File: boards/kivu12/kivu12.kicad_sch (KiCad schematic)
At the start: 26 parts, among them J1 P1, J10 SD, J11 GND, J12 LX2, J2 CIX, J3 BX, J4 LX1, J5 ANALOG, J6 POWER2, J7 BX, J9 POWER1

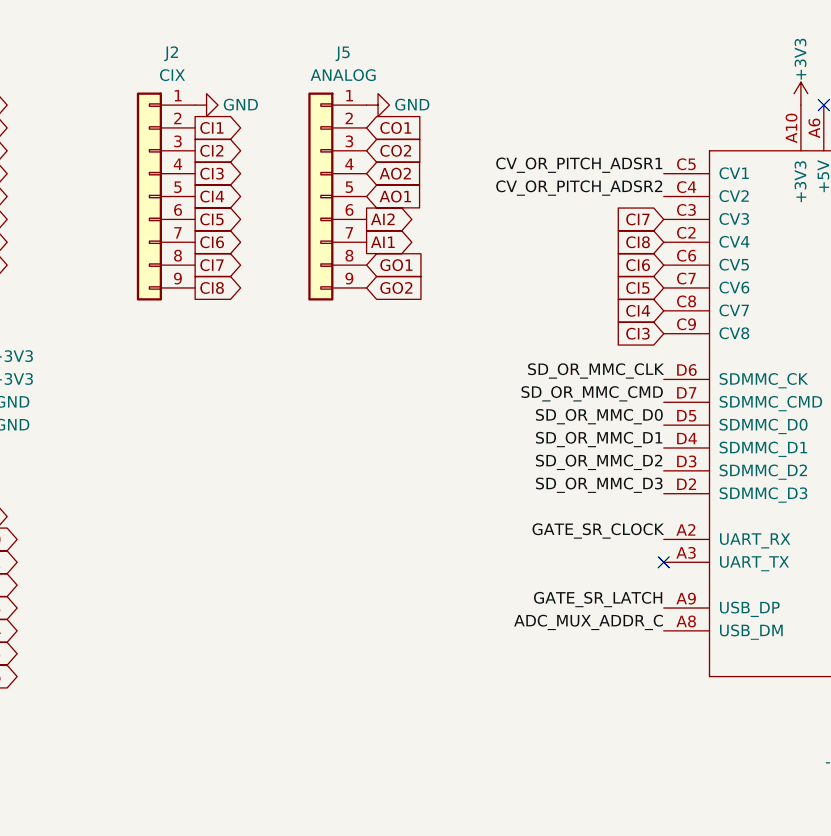
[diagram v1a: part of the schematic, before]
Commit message: Add normalization probe pin
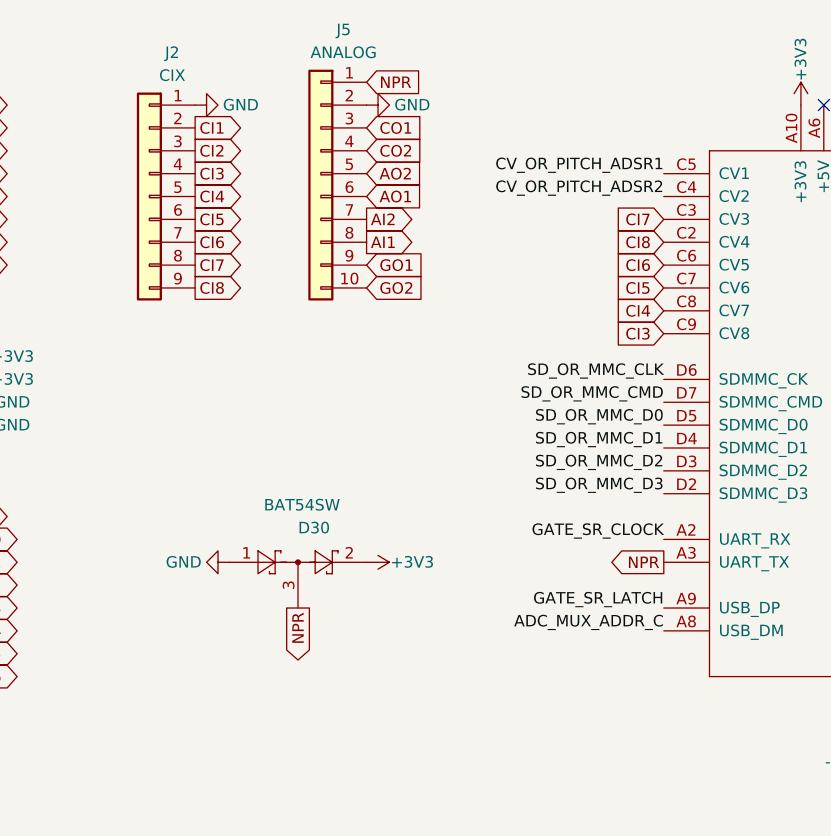
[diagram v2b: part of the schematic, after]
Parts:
- added D30: BAT54SW, Package_TO_SOT_SMD:SOT-323_SC-70, symbol Diode:BAT54SW
- J5: footprint Connector_PinSocket_2.54mm:PinSocket_1x09_P2.54mm_Vertical -> Connector_PinSocket_2.54mm:PinSocket_1x10_P2.54mm_Vertical; symbol Connector_Generic:Conn_01x09 -> Connector_Generic:Conn_01x10; DistLink https://www.digikey.de/en/products/detail/sullins-connector-solutions/PPTC091LFBN-RC/810148 -> https://www.digikey.de/en/products/detail/sullins-connector-solutions/PPTC101LFBN-RC/810149; DistPartNumber S7007-ND -> S7008-ND
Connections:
- net +3V3: now also D30.2
- net AI1: now also J5.8 (Pin_8); no longer J5.7 (Pin_7)
- net AI2: now also J5.7 (Pin_7); no longer J5.6 (Pin_6)
- net AO1: now also J5.6 (Pin_6); no longer J5.5 (Pin_5)
- net AO2: now also J5.5 (Pin_5); no longer J5.4 (Pin_4)
- net CO1: now also J5.3 (Pin_3); no longer J5.2 (Pin_2)
- net CO2: now also J5.4 (Pin_4); no longer J5.3 (Pin_3)
- net GND: now also J5.2 (Pin_2), D30.1; no longer J5.1 (Pin_1)
- net GO1: now also J5.9 (Pin_9); no longer J5.8 (Pin_8)
- net GO2: now also J5.10 (Pin_10); no longer J5.9 (Pin_9)
- net NPR: now reaches DPSM1.A3 (UART_TX)
- net NPR: now also J5.1 (Pin_1), D30.3
- no-connect marks 2 -> 1
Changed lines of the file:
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@@
   (paper "A4")
   (no_connect (at 176.53 26.67))
-  (no_connect (at 158.75 77.47))
   (text "Just needed for BOM\nThey are:\n- 4x 2x5 female socket for the DPSM\n- 1x 1x36 Male header\n- 8x Jumpers"
     (at 246.38 57.15 0)
@@
     )
   )
+  (global_label "NPR" (shape output) (at 158.75 77.47 180) (fields_autoplaced)
+    (effects (font (size 1.27 1.27)) (justify right))
+    (property "Intersheet References" "${INTERSHEET_REFS}" (id 0) (at 152.5553 77.3906 0)
+      (effects (font (size 1.27 1.27)) (justify right) hide)
+    )
+  )
   (global_label "CI3" (shape output) (at 106.68 34.29 0) (fields_autoplaced)
     (effects (font (size 1.27 1.27)) (justify left))
@@
     )
   )
+  (global_label "NPR" (shape input) (at 125.73 24.13 0) (fields_autoplaced)
+    (effects (font (size 1.27 1.27)) (justify left))
+    (property "Intersheet References" "${INTERSHEET_REFS}" (id 0) (at 131.9247 24.0506 0)
+      (effects (font (size 1.27 1.27)) (justify left) hide)
+    )
+  )
   (global_label "L10" (shape output) (at 158.75 139.7 0) (fields_autoplaced)
     (effects (font (size 1.27 1.27)) (justify left))
@@
     )
   )
+  (global_label "NPR" (shape output) (at 118.11 82.55 270) (fields_autoplaced)
+    (effects (font (size 1.27 1.27)) (justify right))
+    (property "Intersheet References" "${INTERSHEET_REFS}" (id 0) (at 118.0306 88.7447 90)
+      (effects (font (size 1.27 1.27)) (justify right) hide)
+    )
+  )
   (global_label "L11" (shape input) (at 58.42 59.69 0) (fields_autoplaced)
     (effects (font (size 1.27 1.27)) (justify left))
@@
     (pin "8")
   )
-  (symbol (lib_id "Connector_Generic:Conn_01x09") (at 120.65 36.83 0) (mirror y) (unit 1)
+  (symbol (lib_id "Connector_Generic:Conn_01x10") (at 120.65 34.29 0) (mirror y) (unit 1)
     (in_bom yes) (on_board yes)
-    (property "Reference" "J5" (id 0) (at 123.19 21.59 0)
+    (property "Reference" "J5" (id 0) (at 123.19 19.05 0)
       (effects (font (size 1.27 1.27)) (justify bottom))
     )
-    (property "Value" "ANALOG" (id 1) (at 123.19 24.13 0)
+    (property "Value" "ANALOG" (id 1) (at 123.19 21.59 0)
       (effects (font (size 1.27 1.27)) (justify bottom))
     )
-    (property "Footprint" "Connector_PinSocket_2.54mm:PinSocket_1x09_P2.54mm_Vertical" (id 2) (at 120.65 36.83 0)
+    (property "Footprint" "Connector_PinSocket_2.54mm:PinSocket_1x10_P2.54mm_Vertical" (id 2) (at 120.65 34.29 0)
       (effects (font (size 1.27 1.27)) hide)
     )
-    (property "Datasheet" "~" (id 3) (at 120.65 36.83 0)
+    (property "Datasheet" "~" (id 3) (at 120.65 34.29 0)
       (effects (font (size 1.27 1.27)) hide)
     )
-    (property "Device" "Female Socket" (id 4) (at 120.65 36.83 0)
+    (property "Device" "Female Socket" (id 4) (at 120.65 34.29 0)
       (effects (font (size 1.27 1.27)) hide)
     )
-    (property "Description" "CONN HDR 9POS 0.1 TIN PCB" (id 5) (at 120.65 36.83 0)
+    (property "Description" "CONN HDR 10POS 0.1 TIN PCB" (id 5) (at 120.65 34.29 0)
       (effects (font (size 1.27 1.27)) hide)
     )
-    (property "Place" "No" (id 6) (at 120.65 36.83 0)
+    (property "Place" "No" (id 6) (at 120.65 34.29 0)
       (effects (font (size 1.27 1.27)) hide)
     )
-    (property "Dist" "Digikey" (id 7) (at 120.65 36.83 0)
+    (property "Dist" "Digikey" (id 7) (at 120.65 34.29 0)
       (effects (font (size 1.27 1.27)) hide)
     )
-    (property "DistPartNumber" "S7007-ND" (id 8) (at 120.65 36.83 0)
+    (property "DistPartNumber" "S7008-ND" (id 8) (at 120.65 34.29 0)
       (effects (font (size 1.27 1.27)) hide)
     )
-    (property "DiskLink" "" (id 9) (at 120.65 36.83 0)
+    (property "DiskLink" "" (id 9) (at 120.65 34.29 0)
       (effects (font (size 1.27 1.27)) hide)
     )
-    (property "DistLink" "https://www.digikey.de/en/products/detail/sullins-connector-solutions/PPTC091LFBN-RC/810148" (id 10) (at 120.65 36.83 0)
+    (property "DistLink" "https://www.digikey.de/en/products/detail/sullins-connector-solutions/PPTC101LFBN-RC/810149" (id 10) (at 120.65 34.29 0)
       (effects (font (size 1.27 1.27)) hide)
     )
     (pin "1")
+    (pin "10")
     (pin "2")
     (pin "3")
@@
     )
   )
+  (symbol (lib_id "power:GND") (at 110.49 77.47 270) (unit 1)
+    (in_bom yes) (on_board yes)
+    (property "Reference" "#PWR0109" (id 0) (at 104.14 77.47 0)
+      (effects (font (size 1.27 1.27)) hide)
+    )
+    (property "Value" "GND" (id 1) (at 105.41 77.47 90))
+    (property "Footprint" "" (id 2) (at 110.49 77.47 0)
+      (effects (font (size 1.27 1.27)) hide)
+    )
+    (property "Datasheet" "" (id 3) (at 110.49 77.47 0)
+      (effects (font (size 1.27 1.27)) hide)
+    )
+    (pin "1")
+  )
+  (symbol (lib_id "Diode:BAT54SW") (at 118.11 77.47 0) (unit 1)
+    (in_bom yes) (on_board yes)
+    (property "Reference" "D30" (id 0) (at 118.11 73.66 0)
+      (effects (font (size 1.27 1.27)) (justify left))
+    )
+    (property "Value" "BAT54SW" (id 1) (at 114.3 71.12 0)
+      (effects (font (size 1.27 1.27)) (justify left))
+    )
+    (property "Footprint" "Package_TO_SOT_SMD:SOT-323_SC-70" (id 2) (at 120.015 74.295 0)
+      (effects (font (size 1.27 1.27)) (justify left) hide)
+    )
+    (property "Datasheet" "https://www.st.com/content/ccc/resource/technical/document/datasheet/07/50/54/f2/0d/ba/4a/79/CD00001322.pdf/files/CD00001322.pdf/jcr:content/translations/en.CD00001322.pdf" (id 3) (at 115.062 77.47 0)
+      (effects (font (size 1.27 1.27)) hide)
+    )
+    (property "Device" "Diode Array" (id 4) (at 118.11 77.47 0)
+      (effects (font (size 1.27 1.27)) hide)
+    )
+    (property "Package" "SC-70, SOT-323" (id 5) (at 118.11 77.47 0)
+      (effects (font (size 1.27 1.27)) hide)
+    )
+    (property "Description" "DIODE ARRAY SCHOTTKY 40V SOT323" (id 6) (at 118.11 77.47 0)
+      (effects (font (size 1.27 1.27)) hide)
+    )
+    (property "Place" "Yes" (id 7) (at 118.11 77.47 0)
+      (effects (font (size 1.27 1.27)) hide)
+    )
+    (property "Dist" "Digikey" (id 8) (at 118.11 77.47 0)
+      (effects (font (size 1.27 1.27)) hide)
+    )
+    (property "DistPartNumber" "497-14153-1-ND" (id 9) (at 118.11 77.47 0)
+      (effects (font (size 1.27 1.27)) hide)
+    )
+    (property "DiskLink" "" (id 10) (at 118.11 77.47 0)
+      (effects (font (size 1.27 1.27)) hide)
+    )
+    (property "DistLink" "https://www.digikey.de/en/products/detail/stmicroelectronics/BAT54SWFILM/1037674" (id 11) (at 118.11 77.47 0)
+      (effects (font (size 1.27 1.27)) hide)
+    )
+    (pin "1")
+    (pin "2")
+    (pin "3")
+  )
+  (symbol (lib_id "power:+3V3") (at 125.73 77.47 270) (unit 1)
+    (in_bom yes) (on_board yes)
+    (property "Reference" "#PWR0115" (id 0) (at 121.92 77.47 0)
+      (effects (font (size 1.27 1.27)) hide)
+    )
+    (property "Value" "+3V3" (id 1) (at 130.81 77.47 90))
+    (property "Footprint" "" (id 2) (at 125.73 77.47 0)
+      (effects (font (size 1.27 1.27)) hide)
+    )
+    (property "Datasheet" "" (id 3) (at 125.73 77.47 0)
+      (effects (font (size 1.27 1.27)) hide)
+    )
+    (pin "1")
+  )
   (sheet (at 181.61 143.51) (size 27.94 17.78) (fields_autoplaced)
     (stroke (width 0) (type solid) (color 0 0 0 0))
@@
       (reference "#PWR0108") (unit 1) (value "+3V3") (footprint "")
     )
+    (path "/01a659c6-01e4-4c7c-b4cc-21f3b52c9a66"
+      (reference "#PWR0109") (unit 1) (value "GND") (footprint "")
+    )
     (path "/00000000-0000-0000-0000-0000608cf77c"
       (reference "#PWR0110") (unit 1) (value "+12V") (footprint "")
@@
       (reference "#PWR0114") (unit 1) (value "GND") (footprint "")
     )
+    (path "/7c9b9994-95f2-46a1-9c7b-339738e24d9f"
+      (reference "#PWR0115") (unit 1) (value "+3V3") (footprint "")
+    )
     (path "/00000000-0000-0000-0000-000060e3a2bf"
       (reference "#PWR0116") (unit 1) (value "GND") (footprint "")
@@
       (reference "D24") (unit 1) (value "D_Schottky") (footprint "Diode_SMD:D_SOD-123")
     )
+    (path "/537cf7b1-9d1a-4340-be57-7cbf7bc3c576"
+      (reference "D30") (unit 1) (value "BAT54SW") (footprint "Package_TO_SOT_SMD:SOT-323_SC-70")
+    )
     (path "/00000000-0000-0000-0000-0000608c5a2c"
       (reference "DPSM1") (unit 1) (value "DaisyPatchSm_Rev1") (footprint "Socket_DaisyPatchSm:DaisyPatchSm")
@@
     )
     (path "/00000000-0000-0000-0000-00006162f4c0"
-      (reference "J5") (unit 1) (value "ANALOG") (footprint "Connector_PinSocket_2.54mm:PinSocket_1x09_P2.54mm_Vertical")
+      (reference "J5") (unit 1) (value "ANALOG") (footprint "Connector_PinSocket_2.54mm:PinSocket_1x10_P2.54mm_Vertical")
     )
     (path "/00000000-0000-0000-0000-000061625402"

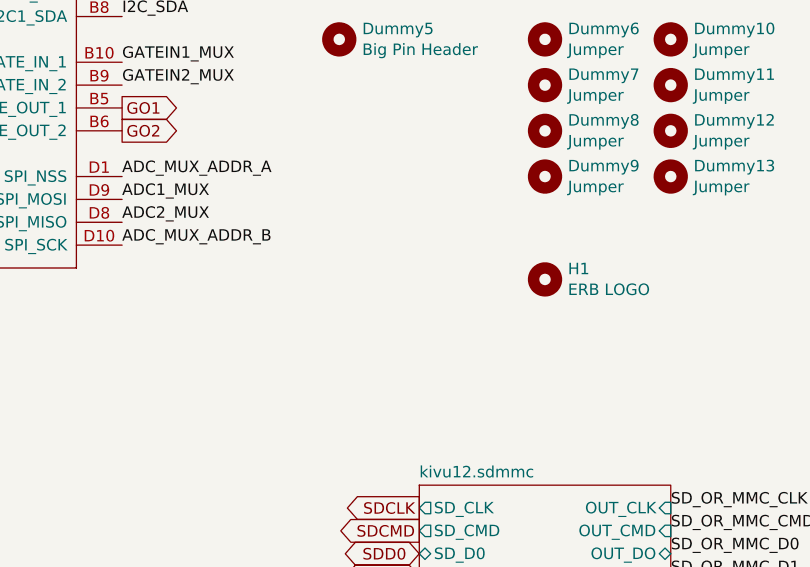
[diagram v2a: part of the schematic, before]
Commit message: Add support for jlcpcb pcba service
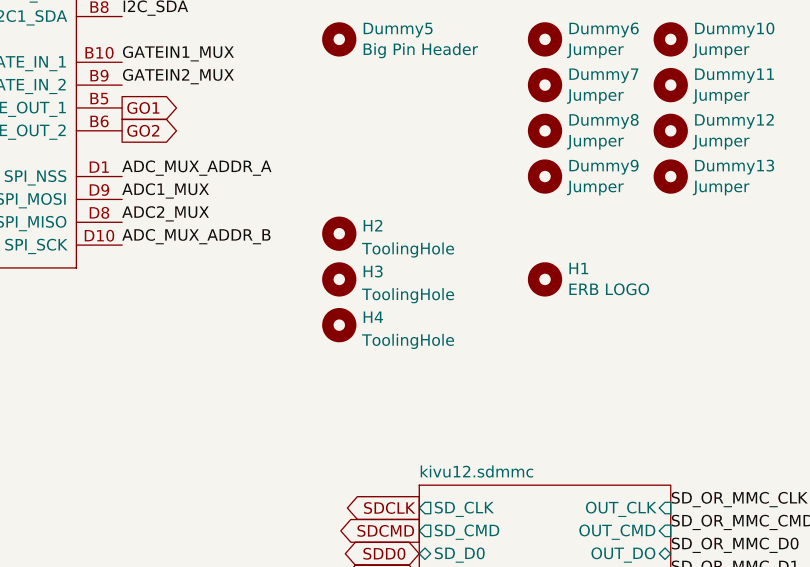
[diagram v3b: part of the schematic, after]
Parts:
- added H2, H3, H4: ToolingHole, JlcPcbToolingHole:JlcPcbToolingHole, symbol Mechanical:MountingHole
- D30: JlcPcbPartNumber (none) -> C472583; Package SC-70, SOT-323 -> SOT-323-3; ReelRotation (none) -> 180
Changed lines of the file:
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@@
       (effects (font (size 1.27 1.27)) hide)
     )
-    (property "Package" "SC-70, SOT-323" (id 5) (at 118.11 77.47 0)
+    (property "Package" "SOT-323-3" (id 5) (at 118.11 77.47 0)
       (effects (font (size 1.27 1.27)) hide)
     )
@@
     )
     (property "DistLink" "https://www.digikey.de/en/products/detail/stmicroelectronics/BAT54SWFILM/1037674" (id 11) (at 118.11 77.47 0)
+      (effects (font (size 1.27 1.27)) hide)
+    )
+    (property "JlcPcbPartNumber" "C472583" (id 12) (at 118.11 77.47 0)
+      (effects (font (size 1.27 1.27)) hide)
+    )
+    (property "ReelRotation" "180" (id 13) (at 118.11 77.47 0)
       (effects (font (size 1.27 1.27)) hide)
     )
@@
     (pin "3")
   )
+  (symbol (lib_id "Mechanical:MountingHole") (at 228.6 91.44 0) (unit 1)
+    (in_bom yes) (on_board yes) (fields_autoplaced)
+    (property "Reference" "H3" (id 0) (at 231.14 90.6053 0)
+      (effects (font (size 1.27 1.27)) (justify left))
+    )
+    (property "Value" "ToolingHole" (id 1) (at 231.14 93.1422 0)
+      (effects (font (size 1.27 1.27)) (justify left))
+    )
+    (property "Footprint" "JlcPcbToolingHole:JlcPcbToolingHole" (id 2) (at 228.6 91.44 0)
+      (effects (font (size 1.27 1.27)) hide)
+    )
+    (property "Datasheet" "~" (id 3) (at 228.6 91.44 0)
+      (effects (font (size 1.27 1.27)) hide)
+    )
+  )
   (symbol (lib_id "power:+3V3") (at 125.73 77.47 270) (unit 1)
     (in_bom yes) (on_board yes)
@@
     )
     (pin "1")
+  )
+  (symbol (lib_id "Mechanical:MountingHole") (at 228.6 86.36 0) (unit 1)
+    (in_bom yes) (on_board yes) (fields_autoplaced)
+    (property "Reference" "H2" (id 0) (at 231.14 85.5253 0)
+      (effects (font (size 1.27 1.27)) (justify left))
+    )
+    (property "Value" "ToolingHole" (id 1) (at 231.14 88.0622 0)
+      (effects (font (size 1.27 1.27)) (justify left))
+    )
+    (property "Footprint" "JlcPcbToolingHole:JlcPcbToolingHole" (id 2) (at 228.6 86.36 0)
+      (effects (font (size 1.27 1.27)) hide)
+    )
+    (property "Datasheet" "~" (id 3) (at 228.6 86.36 0)
+      (effects (font (size 1.27 1.27)) hide)
+    )
+  )
+  (symbol (lib_id "Mechanical:MountingHole") (at 228.6 96.52 0) (unit 1)
+    (in_bom yes) (on_board yes) (fields_autoplaced)
+    (property "Reference" "H4" (id 0) (at 231.14 95.6853 0)
+      (effects (font (size 1.27 1.27)) (justify left))
+    )
+    (property "Value" "ToolingHole" (id 1) (at 231.14 98.2222 0)
+      (effects (font (size 1.27 1.27)) (justify left))
+    )
+    (property "Footprint" "JlcPcbToolingHole:JlcPcbToolingHole" (id 2) (at 228.6 96.52 0)
+      (effects (font (size 1.27 1.27)) hide)
+    )
+    (property "Datasheet" "~" (id 3) (at 228.6 96.52 0)
+      (effects (font (size 1.27 1.27)) hide)
+    )
   )
   (sheet (at 181.61 143.51) (size 27.94 17.78) (fields_autoplaced)
@@
       (reference "H1") (unit 1) (value "ERB LOGO") (footprint "Logo_Erb:ErbLog.15mm")
     )
+    (path "/c55c6a2b-7145-443e-a402-9d8950328d23"
+      (reference "H2") (unit 1) (value "ToolingHole") (footprint "JlcPcbToolingHole:JlcPcbToolingHole")
+    )
+    (path "/7b1efe6d-d268-4219-8bc1-1852527b62ac"
+      (reference "H3") (unit 1) (value "ToolingHole") (footprint "JlcPcbToolingHole:JlcPcbToolingHole")
+    )
+    (path "/df4ee194-4154-406e-8108-f1271db10eb0"
+      (reference "H4") (unit 1) (value "ToolingHole") (footprint "JlcPcbToolingHole:JlcPcbToolingHole")
+    )
     (path "/00000000-0000-0000-0000-00006095892f/00000000-0000-0000-0000-00006095c792"
